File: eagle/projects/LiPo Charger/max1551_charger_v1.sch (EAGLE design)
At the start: 5 parts

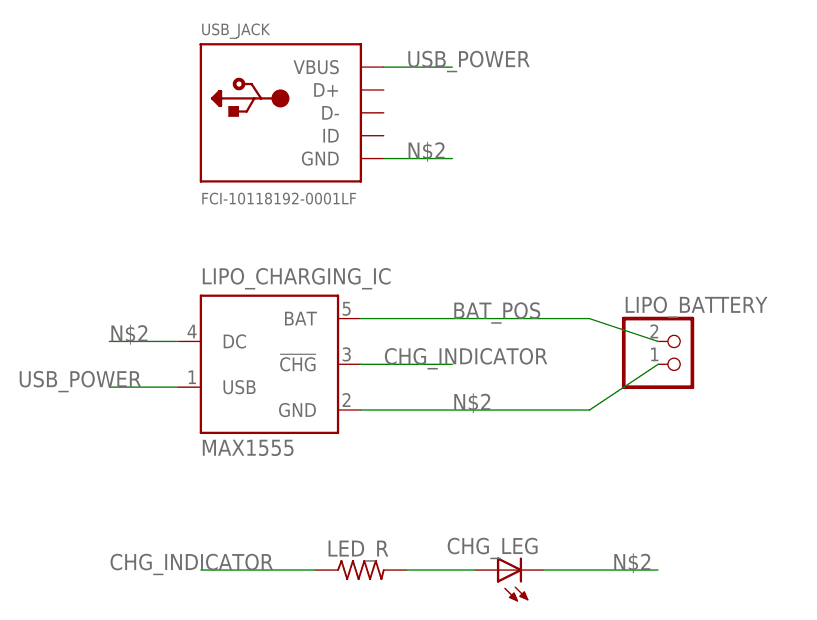
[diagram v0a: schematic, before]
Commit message: Update LiPo Charger with MAX 1551
This board was printed and tested and it seems to work.

It's a bit simple/slow though so a better charger circuit
would probably be advantageous in the future.  Plus the
MAX1551 charger ICs are expensive ~$2 each.

However, it works!  So I'm saving these designs for later

Signed-off-by: Rave Strapon <ravestrapon@gmail.com>
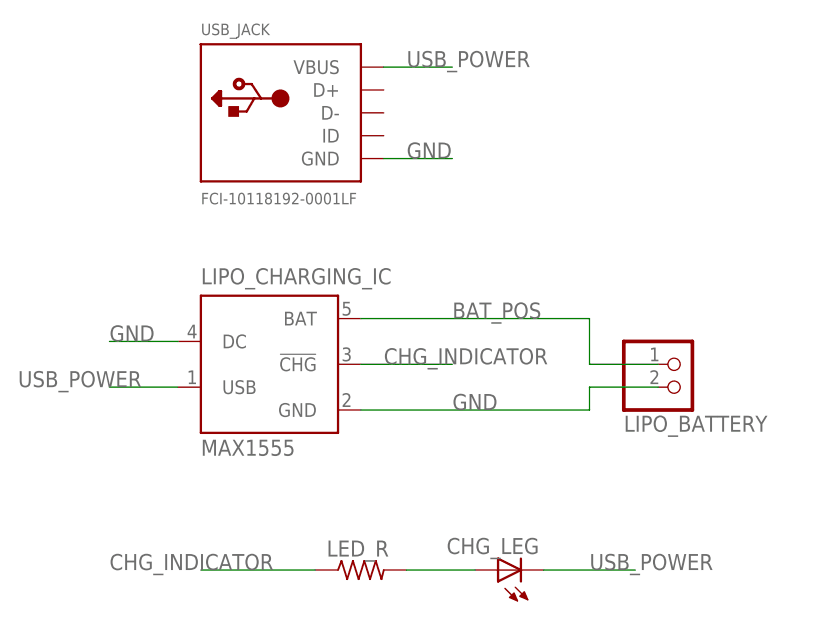
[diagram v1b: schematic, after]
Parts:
- LED_R: device rcl:R-US_0207/10 -> rcl:R-US_0207/2V
- USB_JACK: device cmooney:FCI-10118192-0001LF -> ravestrapon:FCI-10118192-0001LF
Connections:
- removed net N$2: CHG_LEG.C, LIPO_BATTERY.2, LIPO_CHARGING_IC.DC, LIPO_CHARGING_IC.GND, USB_JACK.GND
- new net GND: LIPO_BATTERY.1, LIPO_CHARGING_IC.DC, LIPO_CHARGING_IC.GND, USB_JACK.GND
- net BAT_POS: now also LIPO_BATTERY.2; no longer LIPO_BATTERY.1
- net USB_POWER: now also CHG_LEG.C
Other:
- moved on the sheet: LIPO_BATTERY
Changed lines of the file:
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@@
 <?xml version="1.0" encoding="utf-8"?>
 <!DOCTYPE eagle SYSTEM "eagle.dtd">
-<eagle version="8.4.2">
+<eagle version="8.4.1">
 <drawing>
 <settings>
@@
 <part name="LIPO_CHARGING_IC" library="maxim" library_urn="urn:adsk.eagle:library:269" deviceset="MAX1555" device="" package3d_urn="urn:adsk.eagle:package:17526/1"/>
 <part name="LIPO_BATTERY" library="adafruit" library_urn="urn:adsk.eagle:library:420" deviceset="JST_2PIN" device="-SMT-RA"/>
-<part name="USB_JACK" library="cmooney" deviceset="FCI-10118192-0001LF" device=""/>
-<part name="LED_R" library="rcl" library_urn="urn:adsk.eagle:library:334" deviceset="R-US_" device="0207/10" package3d_urn="urn:adsk.eagle:package:23491/1"/>
 <part name="CHG_LEG" library="adafruit" library_urn="urn:adsk.eagle:library:420" deviceset="LED" device="3MM"/>
+<part name="USB_JACK" library="ravestrapon" deviceset="FCI-10118192-0001LF" device=""/>
+<part name="LED_R" library="rcl" library_urn="urn:adsk.eagle:library:334" deviceset="R-US_" device="0207/2V" package3d_urn="urn:adsk.eagle:package:23490/1"/>
 </parts>
 <sheets>
@@
 <instances>
 <instance part="LIPO_CHARGING_IC" gate="G$1" x="50.8" y="35.56"/>
-<instance part="LIPO_BATTERY" gate="G$1" x="96.52" y="35.56"/>
+<instance part="LIPO_BATTERY" gate="G$1" x="96.52" y="35.56" rot="MR180"/>
+<instance part="CHG_LEG" gate="G$1" x="76.2" y="12.7" rot="R90"/>
 <instance part="USB_JACK" gate="G$1" x="53.34" y="63.5"/>
 <instance part="LED_R" gate="G$1" x="60.96" y="12.7"/>
-<instance part="CHG_LEG" gate="G$1" x="76.2" y="12.7" rot="R90"/>
 </instances>
 <busses>
@@
 <pinref part="LIPO_CHARGING_IC" gate="G$1" pin="BAT"/>
 <wire x1="60.96" y1="40.64" x2="86.36" y2="40.64" width="0.1524" layer="91"/>
-<pinref part="LIPO_BATTERY" gate="G$1" pin="1"/>
-<wire x1="86.36" y1="40.64" x2="93.98" y2="38.1" width="0.1524" layer="91"/>
 <label x="71.12" y="40.64" size="1.778" layer="95"/>
-</segment>
-</net>
-<net name="N$2" class="0">
+<pinref part="LIPO_BATTERY" gate="G$1" pin="2"/>
+<wire x1="93.98" y1="35.56" x2="86.36" y2="35.56" width="0.1524" layer="91"/>
+<wire x1="86.36" y1="35.56" x2="86.36" y2="40.64" width="0.1524" layer="91"/>
+</segment>
+</net>
+<net name="GND" class="0">
 <segment>
 <pinref part="LIPO_CHARGING_IC" gate="G$1" pin="GND"/>
 <wire x1="60.96" y1="30.48" x2="86.36" y2="30.48" width="0.1524" layer="91"/>
-<pinref part="LIPO_BATTERY" gate="G$1" pin="2"/>
-<wire x1="86.36" y1="30.48" x2="93.98" y2="35.56" width="0.1524" layer="91"/>
 <label x="71.12" y="30.48" size="1.778" layer="95"/>
+<pinref part="LIPO_BATTERY" gate="G$1" pin="1"/>
+<wire x1="86.36" y1="30.48" x2="86.36" y2="33.02" width="0.1524" layer="91"/>
+<wire x1="86.36" y1="33.02" x2="93.98" y2="33.02" width="0.1524" layer="91"/>
 </segment>
 <segment>
@@
 </segment>
 <segment>
-<pinref part="USB_JACK" gate="G$1" pin="GND"/>
 <wire x1="63.5" y1="58.42" x2="71.12" y2="58.42" width="0.1524" layer="91"/>
 <label x="66.04" y="58.42" size="1.778" layer="95"/>
-</segment>
-<segment>
-<pinref part="CHG_LEG" gate="G$1" pin="C"/>
-<wire x1="81.28" y1="12.7" x2="93.98" y2="12.7" width="0.1524" layer="91"/>
-<label x="88.9" y="12.7" size="1.778" layer="95"/>
+<pinref part="USB_JACK" gate="G$1" pin="GND"/>
 </segment>
 </net>
 <net name="USB_POWER" class="0">
 <segment>
-<pinref part="USB_JACK" gate="G$1" pin="VBUS"/>
 <wire x1="63.5" y1="68.58" x2="71.12" y2="68.58" width="0.1524" layer="91"/>
 <label x="66.04" y="68.58" size="1.778" layer="95"/>
+<pinref part="USB_JACK" gate="G$1" pin="VBUS"/>
 </segment>
 <segment>
@@
 <label x="22.86" y="33.02" size="1.778" layer="95"/>
 </segment>
+<segment>
+<pinref part="CHG_LEG" gate="G$1" pin="C"/>
+<wire x1="81.28" y1="12.7" x2="91.44" y2="12.7" width="0.1524" layer="91"/>
+<label x="86.36" y="12.7" size="1.778" layer="95"/>
+</segment>
 </net>
 <net name="N$1" class="0">
 <segment>
-<pinref part="LED_R" gate="G$1" pin="2"/>
 <pinref part="CHG_LEG" gate="G$1" pin="A"/>
 <wire x1="73.66" y1="12.7" x2="66.04" y2="12.7" width="0.1524" layer="91"/>
+<pinref part="LED_R" gate="G$1" pin="2"/>
 </segment>
 </net>
@@
 </segment>
 <segment>
-<pinref part="LED_R" gate="G$1" pin="1"/>
 <wire x1="55.88" y1="12.7" x2="43.18" y2="12.7" width="0.1524" layer="91"/>
 <label x="33.02" y="12.7" size="1.778" layer="95"/>
-</segment>
-</net>
+<pinref part="LED_R" gate="G$1" pin="1"/>
+</segment>
+</net>
